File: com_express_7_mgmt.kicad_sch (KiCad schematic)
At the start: 78 parts, among them J12 Plug_Bus_CE7_EPT_401-51501-51, J13 PinHeader_1x3_P2.54mm_Drill1.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, J14 PinHeader_1x3_P2.54mm_Drill1.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, Q11 BSS138-7-F, Q12 BSS138-7-F, SW1 SW_1-1825027-1_THT, SW2 SW_1-1825027-1_THT, U30 74AUP2G132, U31 M24C64-F_DFN8, U32 TPS3840PL30DBVR, U33 74AUP2G132, U34 MAX16150A_SOT, U35 74AUP2G132, U36 W25Q32FV_SOIC-8

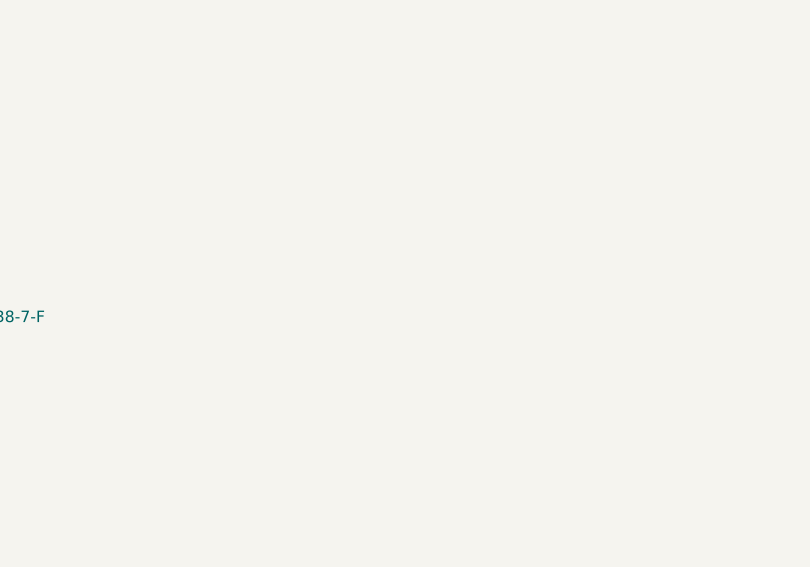
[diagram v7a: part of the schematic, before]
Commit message: [#58137] Add input voltage and buttons ESD protection
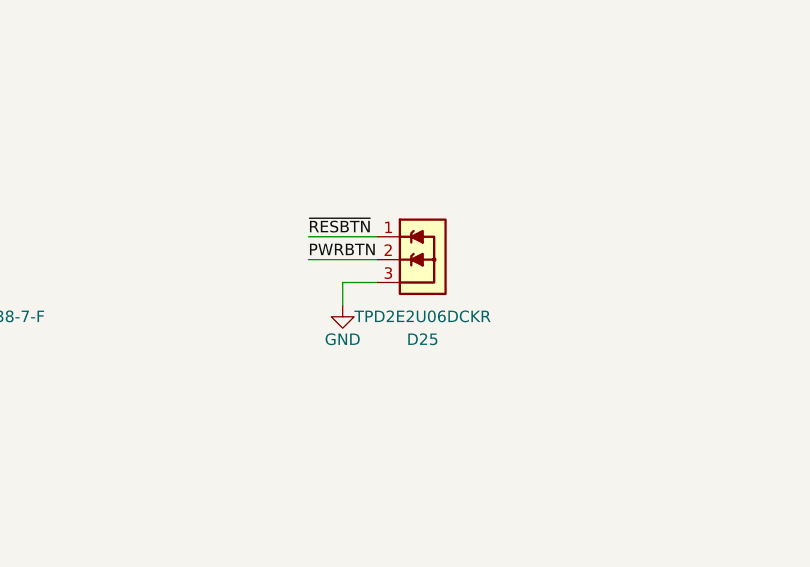
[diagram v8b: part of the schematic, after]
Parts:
- added D25: TPD2E2U06DCKR, antmicro-footprints:SC70-3, symbol antmicroTVSDiodes:TPD2E2U06DCKR
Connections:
- net GND: now also D25.3
- net PWRBTN: now also D25.2
- net ~{RESBTN}: now also D25.1
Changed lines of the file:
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@@
     (stroke (width 0) (type default))
   )
+  (wire (pts (xy 346.71 139.7) (xy 346.71 137.16))
+    (stroke (width 0) (type default))
+  )
   (wire (pts (xy 364.49 57.15) (xy 363.22 57.15))
     (stroke (width 0) (type default))
@@
     (stroke (width 0) (type default))
   )
+  (wire (pts (xy 346.71 137.16) (xy 350.52 137.16))
+    (stroke (width 0) (type default))
+  )
   (wire (pts (xy 83.82 215.9) (xy 76.2 215.9))
     (stroke (width 0) (type default))
@@
     (stroke (width 0) (type default))
   )
+  (wire (pts (xy 342.9 132.08) (xy 350.52 132.08))
+    (stroke (width 0) (type default))
+  )
   (wire (pts (xy 356.87 193.04) (xy 382.27 193.04))
     (stroke (width 0) (type default))
@@
     (stroke (width 0) (type default))
   )
+  (wire (pts (xy 342.9 134.62) (xy 350.52 134.62))
+    (stroke (width 0) (type default))
+  )
   (wire (pts (xy 76.2 264.16) (xy 92.71 264.16))
     (stroke (width 0) (type default))
@@
     (effects (font (size 1.27 1.27)) (justify right bottom))
   )
+  (label "PWRBTN" (at 342.9 134.62 0) (fields_autoplaced)
+    (effects (font (size 1.27 1.27)) (justify left bottom))
+  )
   (label "I2C.SDA" (at 222.25 214.63 180) (fields_autoplaced)
     (effects (font (size 1.27 1.27)) (justify right bottom))
   )
+  (label "~{RESBTN}" (at 342.9 132.08 0) (fields_autoplaced)
+    (effects (font (size 1.27 1.27)) (justify left bottom))
+  )
   (label "SPI.MOSI" (at 328.93 205.74 0) (fields_autoplaced)
     (effects (font (size 1.27 1.27)) (justify left bottom))
@@
     )
   )
+  (symbol (lib_id "antmicroTVSDiodes:TPD2E2U06DCKR") (at 350.52 132.08 0) (unit 1)
+    (in_bom yes) (on_board yes) (dnp no)
+    (property "Reference" "D25" (at 355.6 143.51 0)
+      (effects (font (size 1.27 1.27) (thickness 0.15)))
+    )
+    (property "Value" "TPD2E2U06DCKR" (at 355.6 140.97 0)
+      (effects (font (size 1.27 1.27) (thickness 0.15)))
+    )
+    (property "Footprint" "antmicro-footprints:SC70-3" (at 364.49 132.715 0)
+      (effects (font (size 1.27 1.27) (thickness 0.15)) (justify left bottom) hide)
+    )
+    (property "Datasheet" "https://www.ti.com/lit/ds/symlink/tpd2e2u06.pdf?ts=1706006131823&ref_url=https%253A%252F%252Fwww.ti.com%252Finterface%252Fdiodes%252Fesd-protection-diodes%252Fproducts.html" (at 364.49 135.255 0)
+      (effects (font (size 1.27 1.27) (thickness 0.15)) (justify left bottom) hide)
+    )
+    (property "MPN" "TPD2E2U06DCKR" (at 364.49 137.795 0)
+      (effects (font (size 1.27 1.27) (thickness 0.15)) (justify left bottom) hide)
+    )
+    (property "Manufacturer" "Texas Instruments" (at 364.49 140.335 0)
+      (effects (font (size 1.27 1.27) (thickness 0.15)) (justify left bottom) hide)
+    )
+    (property "Author" "Antmicro" (at 364.49 142.875 0)
+      (effects (font (size 1.27 1.27) (thickness 0.15)) (justify left bottom) hide)
+    )
+    (property "License" "Apache-2.0" (at 364.49 145.415 0)
+      (effects (font (size 1.27 1.27) (thickness 0.15)) (justify left bottom) hide)
+    )
+    (pin "1")
+    (pin "2")
+    (pin "3")
+    (instances
+      (project "com-express-7-baseboard"
+        (path "/1b8c34da-dad5-4b0b-8c4b-45db766c4dfa/ec04a123-aeba-4efb-8d03-9c06245c1fcc"
+          (reference "D25") (unit 1)
+        )
+      )
+    )
+  )
   (symbol (lib_id "antmicropower:GND") (at 104.14 46.99 0) (unit 1)
     (in_bom yes) (on_board yes) (dnp no)
@@
         )
       )
+    )
+  )
+  (symbol (lib_id "antmicropower:GND") (at 346.71 139.7 0) (unit 1)
+    (in_bom yes) (on_board yes) (dnp no)
+    (property "Reference" "#PWR0448" (at 355.6 142.24 0)
+      (effects (font (size 1.27 1.27) (thickness 0.15)) (justify left bottom) hide)
+    )
+    (property "Value" "GND" (at 346.71 143.51 0)
+      (effects (font (size 1.27 1.27) (thickness 0.15)))
+    )
+    (property "Footprint" "" (at 355.6 147.32 0)
+      (effects (font (size 1.27 1.27) (thickness 0.15)) (justify left bottom) hide)
+    )
+    (property "Datasheet" "" (at 355.6 152.4 0)
+      (effects (font (size 1.27 1.27) (thickness 0.15)) (justify left bottom) hide)
+    )
+    (property "Author" "Antmicro" (at 355.6 147.32 0)
+      (effects (font (size 1.27 1.27) (thickness 0.15)) (justify left bottom) hide)
+    )
+    (property "License" "Apache-2.0" (at 355.6 149.86 0)
+      (effects (font (size 1.27 1.27) (thickness 0.15)) (justify left bottom) hide)
+    )
+    (pin "1")
+    (instances
+      (project "com-express-7-baseboard"
+        (path "/1b8c34da-dad5-4b0b-8c4b-45db766c4dfa/ec04a123-aeba-4efb-8d03-9c06245c1fcc"
+          (reference "#PWR0448") (unit 1)
+        )
+      )
